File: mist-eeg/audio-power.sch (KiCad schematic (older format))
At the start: 18 parts, among them U6 LT3042xMSE, U7 LT3042xMSE

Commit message: Hooked-up the SoM
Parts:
- renumbered TP3 to TP4, TP4 to TP5
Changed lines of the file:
@@
 5V0 (clean regulator)
 $Comp
-L Connector:TestPoint TP4
+L Connector:TestPoint TP5
 U 1 1 60C25634
 P 3900 2750
-F 0 "TP4" H 3900 3075 50  0000 C CNN
+F 0 "TP5" H 3900 3075 50  0000 C CNN
 F 1 "+1V8_ANA" H 3900 2984 50  0000 C CNN
 F 2 "TestPoint:TestPoint_Pad_D1.0mm" H 4100 2750 50  0001 C CNN
@@
 Connection ~ 3900 2750
 $Comp
-L Connector:TestPoint TP3
+L Connector:TestPoint TP4
 U 1 1 60C2D0B0
 P 3850 6450
-F 0 "TP3" H 3850 6775 50  0000 C CNN
+F 0 "TP4" H 3850 6775 50  0000 C CNN
 F 1 "+5V0_ANA" H 3850 6684 50  0000 C CNN
 F 2 "TestPoint:TestPoint_Pad_D1.0mm" H 4050 6450 50  0001 C CNN

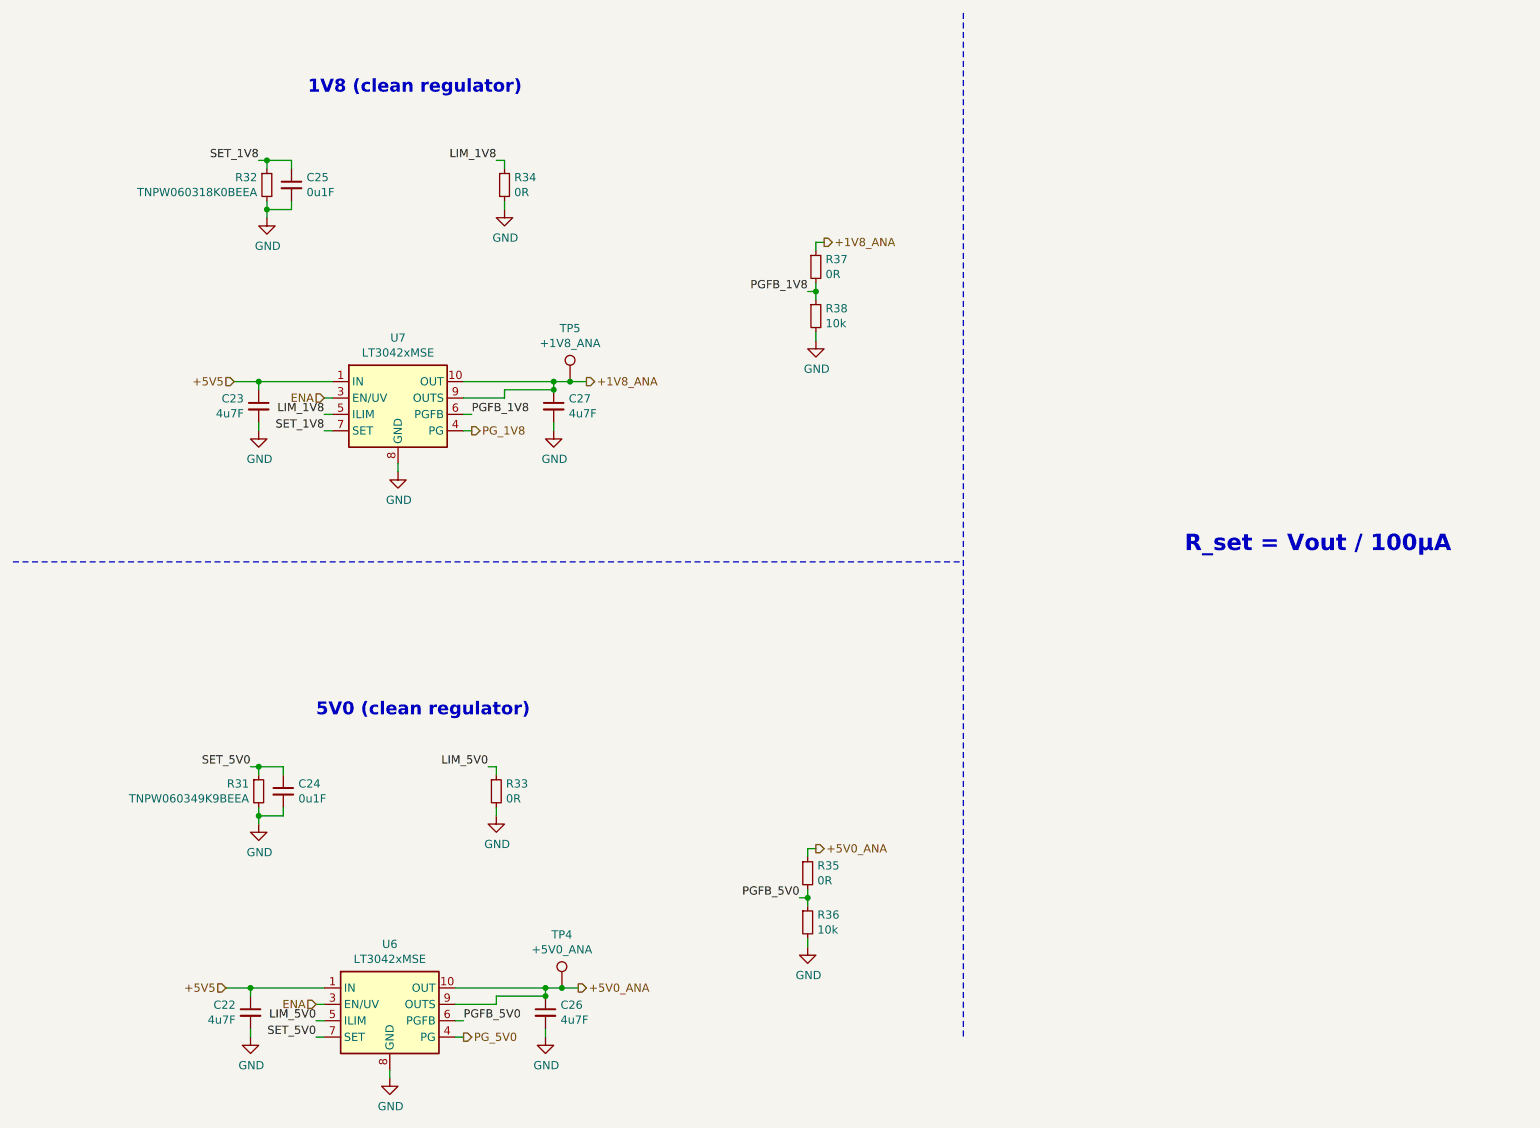
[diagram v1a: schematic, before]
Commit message: Finish schematic and create interface specifications
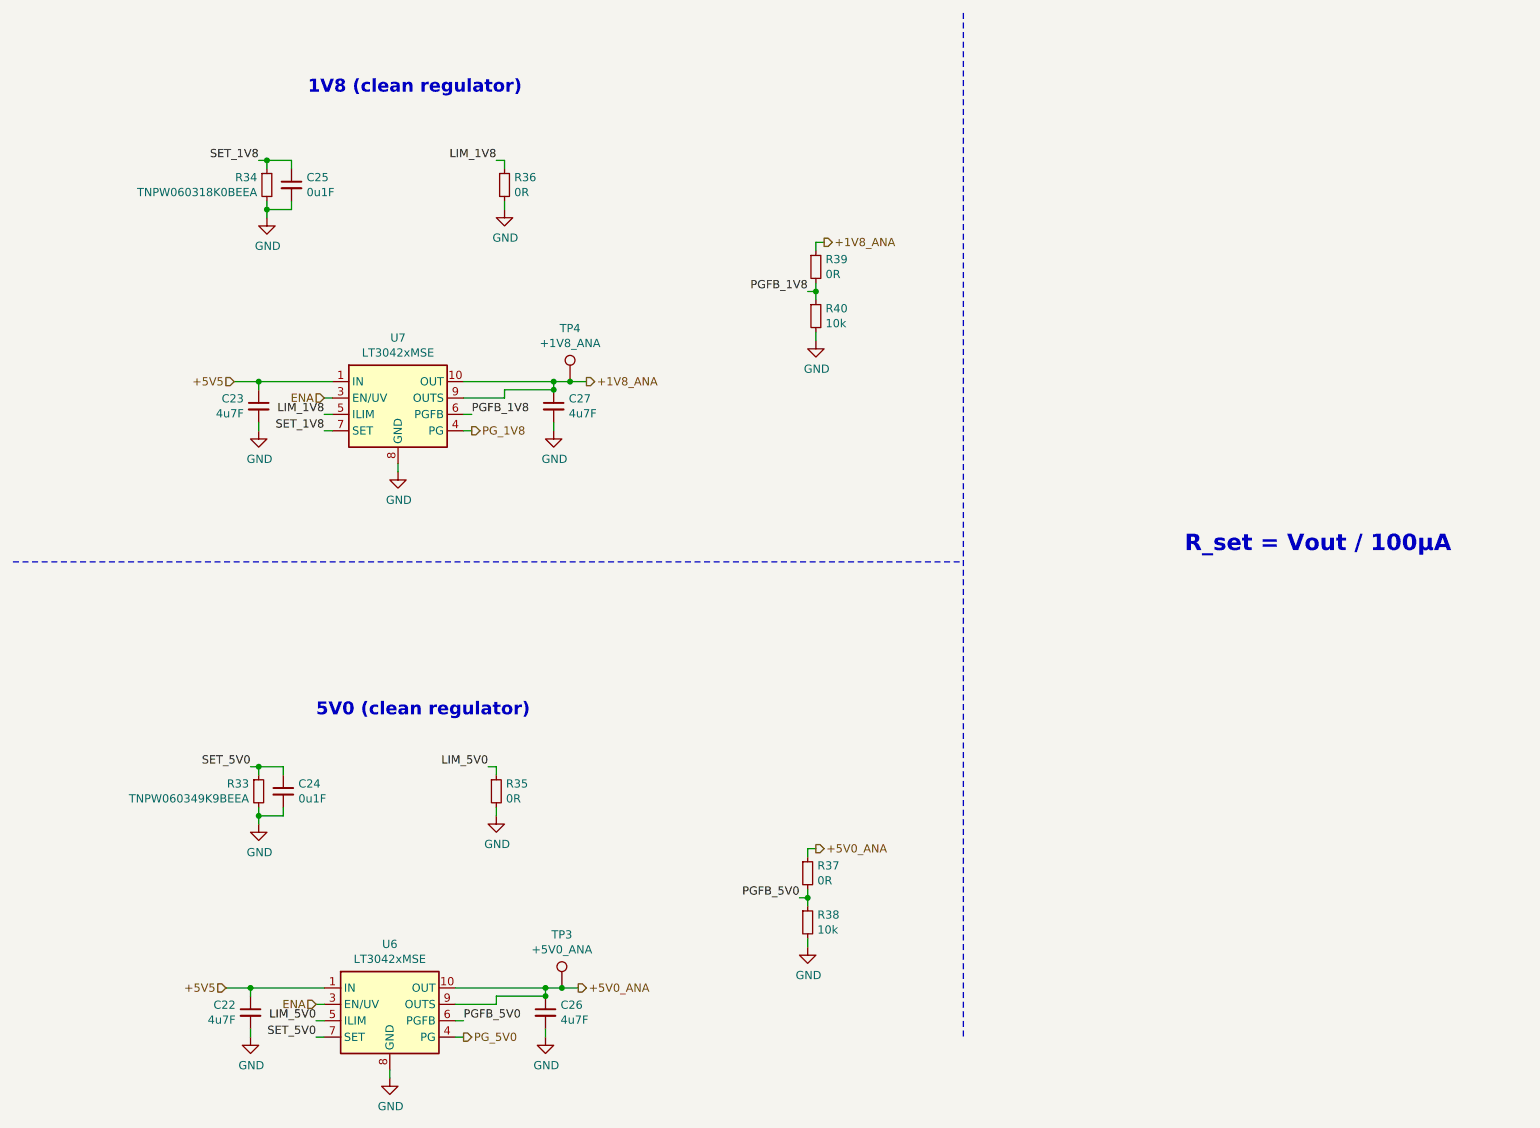
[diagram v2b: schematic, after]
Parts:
- renumbered R31 to R33, R32 to R34, R33 to R35, R34 to R36, R35 to R37, R36 to R38, R37 to R39, R38 to R40, TP4 to TP3, TP5 to TP4
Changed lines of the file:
@@
 	2400 2950 2450 2950
 $Comp
-L Device:R_Small R34
+L Device:R_Small R36
 U 1 1 60CFCD89
 P 3500 1550
-F 0 "R34" H 3559 1596 50  0000 L CNN
+F 0 "R36" H 3559 1596 50  0000 L CNN
 F 1 "0R" H 3559 1505 50  0000 L CNN
 F 2 "Resistor_SMD:R_0603_1608Metric" H 3500 1550 50  0001 C CNN
@@
 $EndComp
 $Comp
-L Device:R_Small R37
+L Device:R_Small R39
 U 1 1 60D00084
 P 5400 2050
-F 0 "R37" H 5459 2096 50  0000 L CNN
+F 0 "R39" H 5459 2096 50  0000 L CNN
 F 1 "0R" H 5459 2005 50  0000 L CNN
 F 2 "Resistor_SMD:R_0603_1608Metric" H 5400 2050 50  0001 C CNN
@@
 $EndComp
 $Comp
-L Device:R_Small R38
+L Device:R_Small R40
 U 1 1 60D0018E
 P 5400 2350
-F 0 "R38" H 5459 2396 50  0000 L CNN
+F 0 "R40" H 5459 2396 50  0000 L CNN
 F 1 "10k" H 5459 2305 50  0000 L CNN
 F 2 "Resistor_SMD:R_0603_1608Metric" H 5400 2350 50  0001 C CNN
@@
 	3500 1700 3500 1650
 $Comp
-L Device:R_Small R32
+L Device:R_Small R34
 U 1 1 60D04DA7
 P 2050 1550
-F 0 "R32" H 1991 1596 50  0000 R CNN
+F 0 "R34" H 1991 1596 50  0000 R CNN
 F 1 "TNPW060318K0BEEA" H 1991 1505 50  0000 R CNN
 F 2 "Resistor_SMD:R_0603_1608Metric" H 2050 1550 50  0001 C CNN
@@
 	2350 6650 2400 6650
 $Comp
-L Device:R_Small R33
+L Device:R_Small R35
 U 1 1 60D64530
 P 3450 5250
-F 0 "R33" H 3509 5296 50  0000 L CNN
+F 0 "R35" H 3509 5296 50  0000 L CNN
 F 1 "0R" H 3509 5205 50  0000 L CNN
 F 2 "Resistor_SMD:R_0603_1608Metric" H 3450 5250 50  0001 C CNN
@@
 $EndComp
 $Comp
-L Device:R_Small R35
+L Device:R_Small R37
 U 1 1 60D64536
 P 5350 5750
-F 0 "R35" H 5409 5796 50  0000 L CNN
+F 0 "R37" H 5409 5796 50  0000 L CNN
 F 1 "0R" H 5409 5705 50  0000 L CNN
 F 2 "Resistor_SMD:R_0603_1608Metric" H 5350 5750 50  0001 C CNN
@@
 $EndComp
 $Comp
-L Device:R_Small R36
+L Device:R_Small R38
 U 1 1 60D6453C
 P 5350 6050
-F 0 "R36" H 5409 6096 50  0000 L CNN
+F 0 "R38" H 5409 6096 50  0000 L CNN
 F 1 "10k" H 5409 6005 50  0000 L CNN
 F 2 "Resistor_SMD:R_0603_1608Metric" H 5350 6050 50  0001 C CNN
@@
 	3450 5400 3450 5350
 $Comp
-L Device:R_Small R31
+L Device:R_Small R33
 U 1 1 60D6454C
 P 2000 5250
-F 0 "R31" H 1941 5296 50  0000 R CNN
+F 0 "R33" H 1941 5296 50  0000 R CNN
 F 1 "TNPW060349K9BEEA" H 1941 5205 50  0000 R CNN
 F 2 "Resistor_SMD:R_0603_1608Metric" H 2000 5250 50  0001 C CNN
@@
 5V0 (clean regulator)
 $Comp
-L Connector:TestPoint TP5
+L Connector:TestPoint TP4
 U 1 1 60C25634
 P 3900 2750
-F 0 "TP5" H 3900 3075 50  0000 C CNN
+F 0 "TP4" H 3900 3075 50  0000 C CNN
 F 1 "+1V8_ANA" H 3900 2984 50  0000 C CNN
 F 2 "TestPoint:TestPoint_Pad_D1.0mm" H 4100 2750 50  0001 C CNN
@@
 Connection ~ 3900 2750
 $Comp
-L Connector:TestPoint TP4
+L Connector:TestPoint TP3
 U 1 1 60C2D0B0
 P 3850 6450
-F 0 "TP4" H 3850 6775 50  0000 C CNN
+F 0 "TP3" H 3850 6775 50  0000 C CNN
 F 1 "+5V0_ANA" H 3850 6684 50  0000 C CNN
 F 2 "TestPoint:TestPoint_Pad_D1.0mm" H 4050 6450 50  0001 C CNN
@@
 ENA
 $Comp
-L power:GND #PWR050
+L power:GND #PWR051
 U 1 1 610B067C
 P 3800 3050
-F 0 "#PWR050" H 3800 2800 50  0001 C CNN
+F 0 "#PWR051" H 3800 2800 50  0001 C CNN
 F 1 "GND" H 3805 2877 50  0000 C CNN
 F 2 "" H 3800 3050 50  0001 C CNN
@@
 $EndComp
 $Comp
-L power:GND #PWR046
+L power:GND #PWR047
 U 1 1 610B0AB0
 P 2850 3300
-F 0 "#PWR046" H 2850 3050 50  0001 C CNN
+F 0 "#PWR047" H 2850 3050 50  0001 C CNN
 F 1 "GND" H 2855 3127 50  0000 C CNN
 F 2 "" H 2850 3300 50  0001 C CNN
@@
 $EndComp
 $Comp
-L power:GND #PWR042
+L power:GND #PWR043
 U 1 1 610B0EE6
 P 2000 3050
-F 0 "#PWR042" H 2000 2800 50  0001 C CNN
+F 0 "#PWR043" H 2000 2800 50  0001 C CNN
 F 1 "GND" H 2005 2877 50  0000 C CNN
 F 2 "" H 2000 3050 50  0001 C CNN
@@
 $EndComp
 $Comp
-L power:GND #PWR052
+L power:GND #PWR053
 U 1 1 610B1308
 P 5400 2500
-F 0 "#PWR052" H 5400 2250 50  0001 C CNN
+F 0 "#PWR053" H 5400 2250 50  0001 C CNN
 F 1 "GND" H 5405 2327 50  0000 C CNN
 F 2 "" H 5400 2500 50  0001 C CNN
@@
 $EndComp
 $Comp
-L power:GND #PWR048
+L power:GND #PWR049
 U 1 1 610B1758
 P 3500 1700
-F 0 "#PWR048" H 3500 1450 50  0001 C CNN
+F 0 "#PWR049" H 3500 1450 50  0001 C CNN
 F 1 "GND" H 3505 1527 50  0000 C CNN
 F 2 "" H 3500 1700 50  0001 C CNN
@@
 $EndComp
 $Comp
-L power:GND #PWR044
+L power:GND #PWR045
 U 1 1 610B1BAA
 P 2050 1750
-F 0 "#PWR044" H 2050 1500 50  0001 C CNN
+F 0 "#PWR045" H 2050 1500 50  0001 C CNN
 F 1 "GND" H 2055 1577 50  0000 C CNN
 F 2 "" H 2050 1750 50  0001 C CNN
@@
 $EndComp
 $Comp
-L power:GND #PWR043
+L power:GND #PWR044
 U 1 1 610B1FD2
 P 2000 5450
-F 0 "#PWR043" H 2000 5200 50  0001 C CNN
+F 0 "#PWR044" H 2000 5200 50  0001 C CNN
 F 1 "GND" H 2005 5277 50  0000 C CNN
 F 2 "" H 2000 5450 50  0001 C CNN
@@
 $EndComp
 $Comp
-L power:GND #PWR047
+L power:GND #PWR048
 U 1 1 610B2412
 P 3450 5400
-F 0 "#PWR047" H 3450 5150 50  0001 C CNN
+F 0 "#PWR048" H 3450 5150 50  0001 C CNN
 F 1 "GND" H 3455 5227 50  0000 C CNN
 F 2 "" H 3450 5400 50  0001 C CNN
@@
 $EndComp
 $Comp
-L power:GND #PWR051
+L power:GND #PWR052
 U 1 1 610B2854
 P 5350 6200
-F 0 "#PWR051" H 5350 5950 50  0001 C CNN
+F 0 "#PWR052" H 5350 5950 50  0001 C CNN
 F 1 "GND" H 5355 6027 50  0000 C CNN
 F 2 "" H 5350 6200 50  0001 C CNN
@@
 $EndComp
 $Comp
-L power:GND #PWR049
+L power:GND #PWR050
 U 1 1 610B2C71
 P 3750 6750
-F 0 "#PWR049" H 3750 6500 50  0001 C CNN
+F 0 "#PWR050" H 3750 6500 50  0001 C CNN
 F 1 "GND" H 3755 6577 50  0000 C CNN
 F 2 "" H 3750 6750 50  0001 C CNN
@@
 $EndComp
 $Comp
-L power:GND #PWR045
+L power:GND #PWR046
 U 1 1 610B30B7
 P 2800 7000
-F 0 "#PWR045" H 2800 6750 50  0001 C CNN
+F 0 "#PWR046" H 2800 6750 50  0001 C CNN
 F 1 "GND" H 2805 6827 50  0000 C CNN
 F 2 "" H 2800 7000 50  0001 C CNN
@@
 $EndComp
 $Comp
-L power:GND #PWR041
+L power:GND #PWR042
 U 1 1 610B34FF
 P 1950 6750
-F 0 "#PWR041" H 1950 6500 50  0001 C CNN
+F 0 "#PWR042" H 1950 6500 50  0001 C CNN
 F 1 "GND" H 1955 6577 50  0000 C CNN
 F 2 "" H 1950 6750 50  0001 C CNN

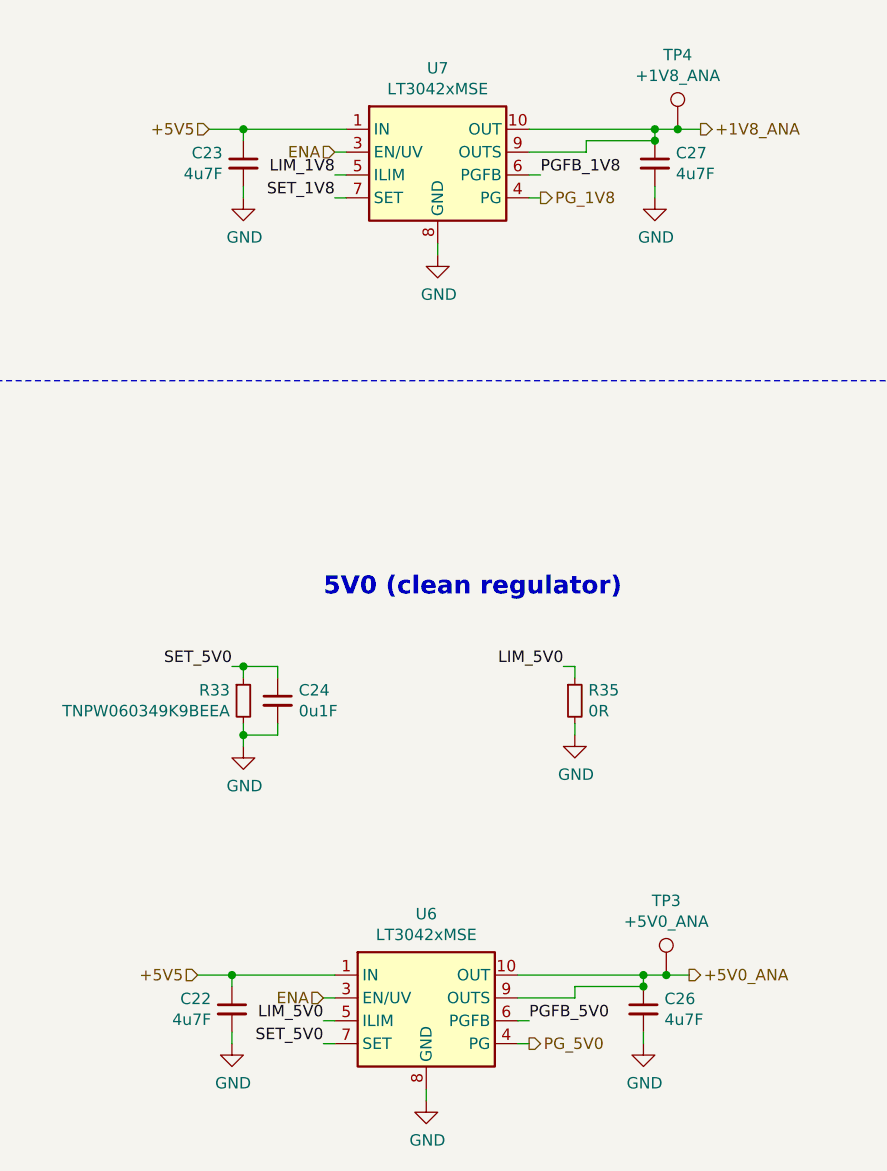
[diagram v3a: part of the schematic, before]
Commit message: Update footprints based upon piece availability & generate manufacturing files
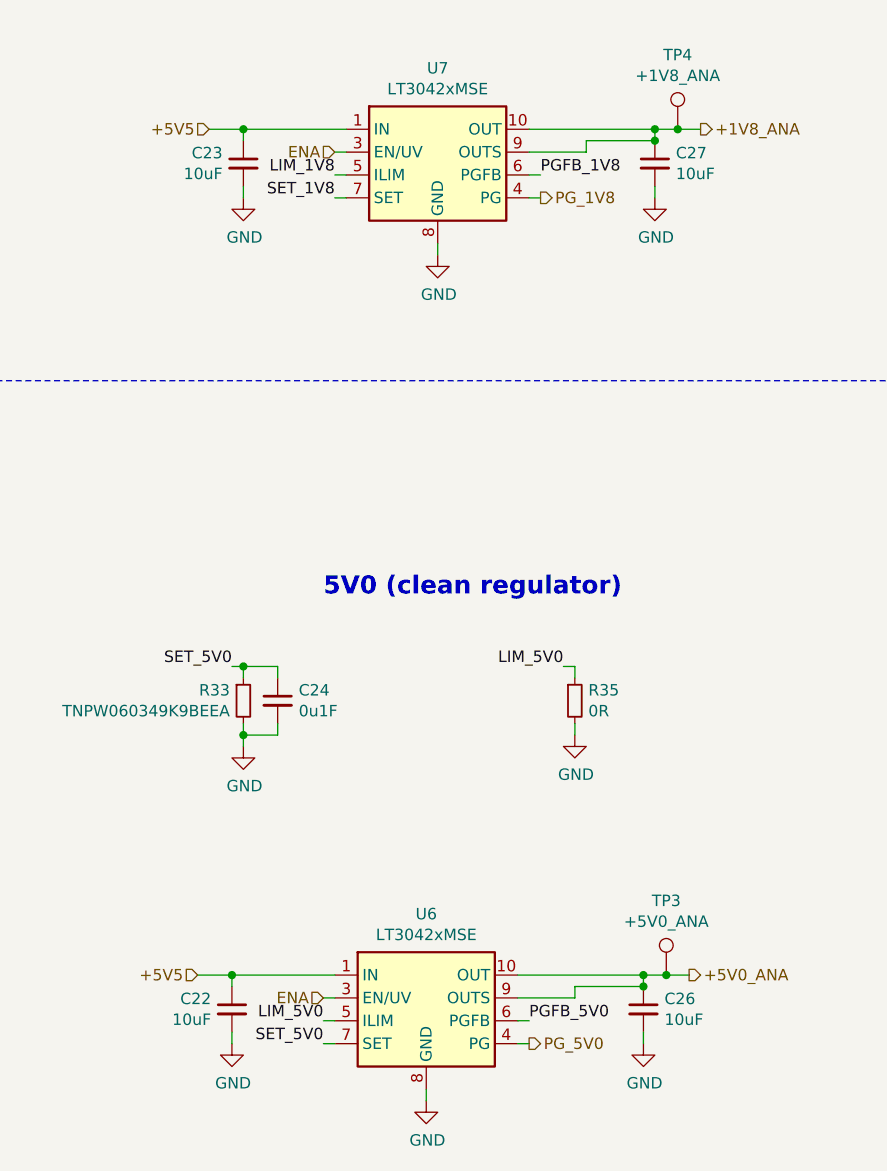
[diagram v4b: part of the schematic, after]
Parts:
- C22, C23, C26, C27: value 4u7F -> 10uF; footprint Capacitor_SMD:C_0201_0603Metric -> Capacitor_SMD:C_0603_1608Metric
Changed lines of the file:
@@
 P 2000 2900
 F 0 "C23" H 1909 2946 50  0000 R CNN
-F 1 "4u7F" H 1909 2855 50  0000 R CNN
-F 2 "Capacitor_SMD:C_0201_0603Metric" H 2000 2900 50  0001 C CNN
+F 1 "10uF" H 1909 2855 50  0000 R CNN
+F 2 "Capacitor_SMD:C_0603_1608Metric" H 2000 2900 50  0001 C CNN
 F 3 "~" H 2000 2900 50  0001 C CNN
 	1    2000 2900
@@
 P 3800 2900
 F 0 "C27" H 3892 2946 50  0000 L CNN
-F 1 "4u7F" H 3892 2855 50  0000 L CNN
-F 2 "Capacitor_SMD:C_0201_0603Metric" H 3800 2900 50  0001 C CNN
+F 1 "10uF" H 3892 2855 50  0000 L CNN
+F 2 "Capacitor_SMD:C_0603_1608Metric" H 3800 2900 50  0001 C CNN
 F 3 "~" H 3800 2900 50  0001 C CNN
 	1    3800 2900
@@
 P 1950 6600
 F 0 "C22" H 1859 6646 50  0000 R CNN
-F 1 "4u7F" H 1859 6555 50  0000 R CNN
-F 2 "Capacitor_SMD:C_0201_0603Metric" H 1950 6600 50  0001 C CNN
+F 1 "10uF" H 1859 6555 50  0000 R CNN
+F 2 "Capacitor_SMD:C_0603_1608Metric" H 1950 6600 50  0001 C CNN
 F 3 "~" H 1950 6600 50  0001 C CNN
 	1    1950 6600
@@
 P 3750 6600
 F 0 "C26" H 3842 6646 50  0000 L CNN
-F 1 "4u7F" H 3842 6555 50  0000 L CNN
-F 2 "Capacitor_SMD:C_0201_0603Metric" H 3750 6600 50  0001 C CNN
+F 1 "10uF" H 3842 6555 50  0000 L CNN
+F 2 "Capacitor_SMD:C_0603_1608Metric" H 3750 6600 50  0001 C CNN
 F 3 "~" H 3750 6600 50  0001 C CNN
 	1    3750 6600
